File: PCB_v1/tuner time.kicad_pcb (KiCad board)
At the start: 4 copper layers, 60 x 40.5 mm, 130 parts, among them IC1 MIC_I2S_SPH0645, IC2 MIC_I2S_SPH0645, IC3 FT2332RL, J1 1051640001, J2 S2B-PH-K-SLFSN, J3 Conn_01x05_Pin, J4 Conn_01x05_Pin, J5 OLED Module Mount, SW7 SW_Push, SW8 SW_Push, U1 BQ25185DLHR, U2 BQ27441-G1, U3 DRV8834PWP, U4 STM32F407VGT6

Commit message: Initial placement draft
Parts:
- removed C32, C33, C34, C38, C39, C42: 100nF, Capacitor_SMD:C_0805_2012Metric
- removed C35, C36, C37: 1uF, Capacitor_SMD:C_0805_2012Metric
- removed C40, C41: 2.2uF, Capacitor_SMD:C_0805_2012Metric
- removed C43, C44: 20pF, Capacitor_SMD:C_0805_2012Metric
- removed C45, C46: 6.8pF, Capacitor_SMD:C_0805_2012Metric
- removed C47: .1uF, Capacitor_SMD:C_0805_2012Metric
- removed IC1, IC2: MIC_I2S_SPH0645, Parts_Library:SPH0645LM4H
- removed IC3: FT2332RL, Parts_Library:SSOP28-LD
- removed JP4, JP5: SB, Jumper:SolderJumper-2_P1.3mm_Bridged_Pad1.0x1.5mm
- removed L1: L, Inductor_SMD:L_0805_2012Metric
- removed R22, R23, R36, R40, R44: 10k, Resistor_SMD:R_0805_2012Metric
- removed R33: 1.5k, Resistor_SMD:R_0805_2012Metric
- removed R34, R35: 47k, Resistor_SMD:R_0805_2012Metric
- removed R37, R38: 0.10, Resistor_SMD:R_0805_2012Metric
- removed R39: 1, Resistor_SMD:R_0805_2012Metric
- removed R41, R45, R56: 510, Resistor_SMD:R_0805_2012Metric
- removed R42: 47, Resistor_SMD:R_0805_2012Metric
- removed R43, R48, R49, R50, R51, R52: 0, Resistor_SMD:R_0805_2012Metric
- removed R46: 330, Resistor_SMD:R_0805_2012Metric
- removed R47: 100, Resistor_SMD:R_0805_2012Metric
- removed R53: 220, Resistor_SMD:R_0805_2012Metric
- removed R54: 220k, Resistor_SMD:R_0805_2012Metric
- removed R55: 100k, Resistor_SMD:R_0805_2012Metric
- removed R57, R58, R59: 680, Resistor_SMD:R_0805_2012Metric
- removed REF**: CONN_B4B-XH-A_JST, Parts_Library:CONN_B4B-XH-A_JST
- added C22: 100nF, Capacitor_SMD:C_0805_2012Metric, F.Cu at (155.1, 75.8)
- added D7: Orange, LED_SMD:LED_0805_2012Metric_Pad1.15x1.40mm_HandSolder, F.Cu at (171.5, 104.6)
- added F1: MFU0805FF01000P500, Parts_Library:FUS_VISHAY_MFU0805_VIS, F.Cu at (154.0, 108.9)
- added FB1: FerriteBead, Inductor_SMD:L_0805_2012Metric, F.Cu at (175.6, 119.8)
- added J10: 1051640001, Parts_Library:CON00906_5_MOL, F.Cu at (155.8, 104.0)
- added J6: Conn_01x05_Pin, Connector_PinHeader_2.54mm:PinHeader_1x05_P2.54mm_Vertical, F.Cu at (225.6, 108.0)
- added J7: Conn_02x04_Odd_Even, Connector_PinHeader_2.00mm:PinHeader_2x04_P2.00mm_Vertical, F.Cu at (191.5, 137.5)
- added J8: B4B-XH-A, Parts_Library:JST_B4B-XH-A, F.Cu at (226.0, 119.0)
- added J9: Conn_ARM_JTAG_SWD_10, Connector_PinHeader_1.27mm:PinHeader_2x05_P1.27mm_Vertical, F.Cu at (186.0, 102.2)
- added JP1: M1, Jumper:SolderJumper-3_P1.3mm_Open_RoundedPad1.0x1.5mm, F.Cu at (191.2, 87.3)
- added JP2: M2, Jumper:SolderJumper-3_P1.3mm_Open_RoundedPad1.0x1.5mm, F.Cu at (191.2, 91.2)
- added RN1: 1k, Parts_Library:RESCAXE50P280X160X55-16N, F.Cu at (166.8, 130.9)
- added RN2: 10k, Parts_Library:RESCAXE50P280X160X55-16N, F.Cu at (171.2, 130.9)
- added RN3: 660, Parts_Library:RESCAXS80P320X160X60-8N, F.Cu at (203.2, 104.8)
- added RV1: 10k, Parts_Library:TRIM_TC33X-2-103E, F.Cu at (205.5, 118.0)
- added SW1: SW_SPST, Parts_Library:JST_B2B-XH-A, F.Cu at (154.0, 121.0)
- added SW2: SW_Push, GT_library:JST_B2B-PH-K-S, F.Cu at (178.5, 136.0)
- added SW3: SW_Push, GT_library:JST_B2B-PH-K-S, F.Cu at (173.5, 136.0)
- added SW4: SW_Push, GT_library:JST_B2B-PH-K-S, F.Cu at (168.5, 136.0)
- added SW5: SW_Push, GT_library:JST_B2B-PH-K-S, F.Cu at (163.5, 136.0)
- added SW6: SW_Push, GT_library:JST_B2B-PH-K-S, F.Cu at (158.5, 136.0)
- added SW9: SW_SPDT, Button_Switch_SMD:SW_SPDT_PCM12, F.Cu at (192.0, 103.5)
- added TP1: ~, TestPoint:TestPoint_THTPad_D1.0mm_Drill0.5mm, F.Cu at (202.5, 126.5)
- added TP10: ~, TestPoint:TestPoint_THTPad_D1.0mm_Drill0.5mm, F.Cu at (185.8, 113.0)
- added TP11: ~, TestPoint:TestPoint_THTPad_D1.0mm_Drill0.5mm, F.Cu at (126.7, 62.4)
- added TP12: ~, TestPoint:TestPoint_THTPad_D1.0mm_Drill0.5mm, F.Cu at (126.7, 65.5)
- added TP13: ~, TestPoint:TestPoint_THTPad_D1.0mm_Drill0.5mm, F.Cu at (183.8, 113.0)
- added TP2: ~, TestPoint:TestPoint_THTPad_D1.0mm_Drill0.5mm, F.Cu at (221.5, 116.5)
- added TP3: TestPoint, TestPoint:TestPoint_THTPad_D1.0mm_Drill0.5mm, F.Cu at (125.7, 101.0)
- added TP4: TestPoint, TestPoint:TestPoint_THTPad_D1.0mm_Drill0.5mm, F.Cu at (125.7, 104.1)
- added TP5: TestPoint, TestPoint:TestPoint_THTPad_D1.0mm_Drill0.5mm, F.Cu at (125.7, 107.1)
- added TP6: TestPoint, TestPoint:TestPoint_THTPad_D1.0mm_Drill0.5mm, F.Cu at (125.7, 110.2)
- added TP7: ~, TestPoint:TestPoint_THTPad_D1.0mm_Drill0.5mm, F.Cu at (120.6, 62.4)
- added TP8: ~, TestPoint:TestPoint_THTPad_D1.0mm_Drill0.5mm, F.Cu at (120.6, 65.5)
- added TP9: ~, TestPoint:TestPoint_THTPad_D1.0mm_Drill0.5mm, F.Cu at (123.6, 62.4)
- added U5: STM32F405RGTx, Package_QFP:LQFP-64_10x10mm_P0.5mm, F.Cu at (187.5, 122.8)
- added U6: ESD9B5.0ST5G, Parts_Library:SODFL1006X40N, F.Cu at (152.0, 108.0)
- added XTAL1: MC-306 32.7680K-E3:ROHS, Parts_Library:SO4_MC-306_SEC, F.Cu at (163.5, 87.7)
- added Y1: ASE-8MHz-L-C-T, Oscillator:Oscillator_SMD_Abracon_ASE-4Pin_3.2x2.5mm, F.Cu at (177.7, 112.9)
- C10: value 10uF -> 100uF; footprint Capacitor_SMD:C_0805_2012Metric -> Parts_Library:CAP_EEE1AA101WR
- C11, C2: value 1uF -> 10uF
- C12: value 0.47uF -> 0.1uF
- C13: value 1uF -> 0.1uF
- C14: value .1uF -> 10uF
- C15, C18: value .1uF -> 20pF
- C16: value .1uF -> 0.01uF
- C17: value .1uF -> 100nF
- C19: value .1uF -> 6.8pF
- C20: value 0.01uF -> 6.8pF
- C21: value 4.7uF -> 10uF
- C23, C26: value 10uF -> 100nF
- C24: value 0.1uF -> 100nF
- C25: value 0.1uF -> 2.2uF
- C27: value 100nF -> 2.2uF
- C3: value 220pF -> 1uF
- C30, C31: value 100nF -> 1uF
- C4: value 220pF -> 0.47uF
- C5: value 0.1uF -> 1uF
- C6: value 10uF -> 100nF; footprint Capacitor_SMD:C_0805_2012Metric -> GT_library:CAP_CA0612_3P2X1P6_YAG
- C7: value 0.1uF -> 100nF; footprint Capacitor_SMD:C_0805_2012Metric -> GT_library:CAP_CA0612_3P2X1P6_YAG
- C8: value 1uF -> 0.01uF
- C9: value 1uF -> 4.7uF
- D1, D2: value YELLOW -> Green
- D3: value Green -> Orange
- D4: value Orange -> Red
- D5: value Red -> Blue
- D6: value Blue -> Green
- J1: value 1051640001 -> Conn_01x03; footprint Parts_Library:CON00906_5_MOL -> Connector_PinHeader_2.54mm:PinHeader_1x03_P2.54mm_Vertical
- J2: value S2B-PH-K-SLFSN -> B6B-PH-K-S; footprint Parts_Library:CONN_S2B-PH-K-S_JST -> GT_library:JST_B6B-PH-K-S
- J3: value Conn_01x05_Pin -> B6B-PH-K-S; footprint Connector_PinHeader_1.00mm:PinHeader_1x05_P1.00mm_Vertical -> GT_library:JST_B6B-PH-K-S
- J4: value Conn_01x05_Pin -> S2B-PH-K-SLFSN; footprint Connector_PinHeader_1.00mm:PinHeader_1x05_P1.00mm_Vertical -> Parts_Library:CONN_S2B-PH-K-S_JST
- J5: value OLED Module Mount -> Conn_01x05_Pin; footprint Connector_PinHeader_2.54mm:PinHeader_1x11_P2.54mm_Vertical -> Connector_PinHeader_2.54mm:PinHeader_1x05_P2.54mm_Vertical
- JP3: value SB -> SLP; footprint Jumper:SolderJumper-2_P1.3mm_Bridged_Pad1.0x1.5mm -> Jumper:SolderJumper-3_P1.3mm_Bridged12_RoundedPad1.0x1.5mm
- R1: value 10k -> 680
- R10: value 0.01 1% -> 100
- R11: value 10k -> 100
- R12: value 1.1k -> 100
- R13, R8, R9: value 5.1k -> 100
- R14, R16, R17: value 100 -> 47k
- R15: value 100 -> 1.5k
- R18: value 100 -> 10k
- R19: value 100 -> 0.10
- R2: value 10k -> 5.1k
- R20: value 10k -> 0.10
- R21: value 10k -> 1
- R24: value 10k -> 220
- R25: value 10k -> 22
- R26, R27, R28: value 1k -> 22
- R29, R30: value 1k -> 10k
- R3: value 68 -> 5.1k
- R31: value 1k -> 680
- R32: value 47k -> 680
- R4: value 68 -> 0.01 1%
- R5: value 0 -> 10k
- R6: value 0 -> 1.1k
- R7: value 300 -> 5.1k
- SW7: footprint Button_Switch_SMD:SW_Push_1P1T_NO_CK_PTS125Sx43PSMTR -> GT_library:JST_B2B-PH-K-S
- SW8: footprint Button_Switch_SMD:SW_Push_1P1T_NO_CK_PTS125Sx43PSMTR -> Parts_Library:SW_TS04-66-65-BK-160-SMT
- U1: value BQ25185DLHR -> C1F 2; footprint Parts_Library:WSON10_DLH_TEX -> Parts_Library:C1_BEL
- U2: value BQ27441-G1 -> BQ25185DLHR; footprint Package_SON:Texas_S-PDSO-N12 -> Parts_Library:WSON10_DLH_TEX
- U3: value DRV8834PWP -> BQ27441-G1; footprint Parts_Library:SOP65P640X120-25N -> Package_SON:Texas_S-PDSO-N12
- U4: value STM32F407VGT6 -> DRV8834PWP; footprint Parts_Library:LQFP100_14x14_STM -> Parts_Library:SOP65P640X120-25N
- moved C17 121.7 mm to (93.5, 68.4)
- moved C19 121.7 mm to (93.5, 74.5)
- moved J2 108.6 mm to (206.5, 130.9), turned to 0 degrees
- moved U1 104.7 mm to (212.0, 108.5), turned to -90 degrees
- moved C25 99.1 mm to (97.9, 74.5)
- moved C8 98.3 mm to (136.8, 62.4)
- moved C20 94.4 mm to (93.5, 77.5)
- moved U4 93.3 mm to (216.2, 116.9), turned to 180 degrees
- moved R30 90.4 mm to (140.3, 143.0)
- moved C2 89.9 mm to (112.5, 115.8)
- moved C3 89.9 mm to (112.5, 118.8)
- moved C4 89.9 mm to (112.5, 121.8)
- moved R14 89.1 mm to (132.4, 62.4)
- moved J1 88.2 mm to (182.9, 137.0), turned to 90 degrees
- moved C27 88.0 mm to (102.4, 62.4)
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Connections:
- C1 pad 1: 3V3 -> GND
- C1 pad 2: GND -> Net-(SW1-A)
- C10 pad 1: VSYS -> VMOT
- C10 pad 2: GND -> AGND
- C11 pad 1: BATT_POS -> VMOT
- C11 pad 2: GND -> AGND
- C12 pad 1: Net-(U2-V_{DD}) -> VMOT
- C12 pad 2: GND -> AGND
- C13 pad 1: GND -> VMOT
- C13 pad 2: VBUS -> AGND
- C14 pad 1: Button1 -> Net-(C14-Pad1)
- C14 pad 2: GND -> AGND
- C15 pad 1: Button2 -> PH0-OSCIN
- C16 pad 1: Button3 -> +3.3V
- C17 pad 1: Button4 -> NRST
- C18 pad 1: Button5 -> PH1-OSCOUT
- C19 pad 1: Button6 -> PC14-OSC32IN
- C2 pad 1: 3V3 -> VSYS
- C20 pad 1: VMOT -> PC15-OSC32OUT
- C20 pad 2: Net-(U3-VCP) -> GND
- C21 pad 1: VINT -> +3.3V
- C23 pad 1: VMOT -> +3.3V
- C24 pad 1: VMOT -> +3.3V
- C25 pad 1: VMOT -> Net-(U5-VCAP_1)
- C26 pad 1: Net-(C26-Pad1) -> +3.3V
- C27 pad 1: GND -> Net-(U5-VCAP_2)
- C27 pad 2: 3V3 -> GND
- C28 pad 1: GND -> +3.3V
- C28 pad 2: 3V3 -> GND
- C29 pad 1: GND -> +3.3VA
- C29 pad 2: 3V3 -> GND
- C3 pad 1: 3V3 -> BATT_POS
- C30 pad 1: GND -> +3.3VA
- C30 pad 2: 3V3 -> GND
- C31 pad 1: GND -> +3.3V
- C31 pad 2: 3V3 -> GND
- C4 pad 1: 3V3 -> Net-(U3-V_{DD})
- C5 pad 1: VBUS -> GND
- C5 pad 2: GND -> VBUS
- C6 pad 1: VBUS -> GND
- C7 pad 1: 3V3 -> Net-(RN1H-R8.1)
- C7 pad 2: GND -> Net-(RN1G-R7.1)
- C8 pad 1: /USB to UART/DTR -> VMOT
- C8 pad 2: GND -> Net-(U4-VCP)
- C9 pad 1: GND -> 3V3
- C9 pad 2: BATT_POS -> AGND
- D1 pad 1: (no net) -> Net-(D1-K)
- D1 pad 2: (no net) -> /Motor/FLT
- D2 pad 1: (no net) -> Net-(D2-K)
- D2 pad 2: (no net) -> PC10
- D3 pad 1: GND -> Net-(D3-K)
- D3 pad 2: Net-(D3-A) -> PC11
- D4 pad 1: GND -> Net-(D4-K)
- D4 pad 2: Net-(D4-A) -> PC12
- D5 pad 1: GND -> Net-(D5-K)
- D5 pad 2: Net-(D5-A) -> PB4
- D6 pad 1: GND -> Net-(D6-K)
- D6 pad 2: Net-(D6-A) -> 3V3
- J1 pad 1: VBUS -> MCU_RX
- J1 pad 2: D- -> MCU_TX
- J1 pad 3: D+ -> GND
- J2 pad 1: GND -> 3V3
- J2 pad 2: BATT_POS -> I2S_WS
- J3 pad 1: unconnected-(J3-Pin_1-Pad1) -> GND
- J3 pad 2: unconnected-(J3-Pin_2-Pad2) -> I2S_WS
- J3 pad 3: Net-(J3-Pin_3) -> I2S_DATA
- J3 pad 4: Net-(J3-Pin_4) -> I2S_BCLK
- J3 pad 5: Net-(J3-Pin_5) -> GND
- J4 pad 1: unconnected-(J4-Pin_1-Pad1) -> GND
- J4 pad 2: unconnected-(J4-Pin_2-Pad2) -> Net-(SW1-A)
- J5 pad 1: MOSI -> unconnected-(J5-Pin_1-Pad1)
- J5 pad 2: SCK -> unconnected-(J5-Pin_2-Pad2)
- J5 pad 3: DC -> Net-(J5-Pin_3)
- J5 pad 4: RST -> Net-(J5-Pin_4)
- J5 pad 5: CS -> Net-(J5-Pin_5)
- JP3 pad 1: Net-(JP3-A) -> 5V
- JP3 pad 2: GND -> /Motor/SLP
- R1 pad 1: GND -> Net-(D1-K)
- R1 pad 2: Net-(IC1-SELECT) -> GND
- R10 pad 1: BATT_POS -> VSYS
- R10 pad 2: VSYS -> Net-(J6-Pin_3)
- R11 pad 1: Net-(U2-BIN) -> 3V3
- R11 pad 2: GND -> Net-(J5-Pin_5)
- R12 pad 1: Net-(U1-ILIM/VSET) -> GND
- R12 pad 2: GND -> Net-(J5-Pin_4)
- R13 pad 1: 3V3 -> VSYS
- R13 pad 2: Net-(U2-GPOUT) -> Net-(J5-Pin_3)
- R14 pad 1: 5V -> 3V3
- R14 pad 2: Net-(J4-Pin_5) -> Net-(U4-CONFIG)
- R15 pad 1: GND -> Net-(U4-FAULT)
- R15 pad 2: Net-(J4-Pin_4) -> /Motor/FLT
- R16 pad 1: VSYS -> Net-(U4-BDECAY)
- R16 pad 2: Net-(J4-Pin_3) -> AGND
- R17 pad 1: 3V3 -> Net-(U4-ADECAY)
- R17 pad 2: Net-(J3-Pin_5) -> AGND
- R18 pad 1: GND -> /Motor/FLT
- R18 pad 2: Net-(J3-Pin_4) -> /Motor/SLP
- R19 pad 1: VSYS -> Net-(U4-BAISEN)
- R19 pad 2: Net-(J3-Pin_3) -> AGND
- R2 pad 2: Net-(IC2-SELECT) -> SCL
- R20 pad 1: 3V3 -> Net-(U4-AISEN)
- R20 pad 2: Net-(R20-Pad2) -> AGND
- R21 pad 1: 3V3 -> VMOT
- R21 pad 2: Net-(R21-Pad2) -> Net-(C14-Pad1)
- R24 pad 1: 3V3 -> Net-(Y1-OUT)
- R24 pad 2: Net-(R24-Pad2) -> PH1-OSCOUT
- R25 pad 1: 3V3 -> NRST
- R25 pad 2: Net-(R25-Pad2) -> Net-(J9-~{RESET})
- R26 pad 1: Net-(R20-Pad2) -> SWCLK
- R26 pad 2: Button1 -> Net-(J9-SWCLK/TCK)
- R27 pad 1: Net-(R21-Pad2) -> SWDIO
- R27 pad 2: Button2 -> Net-(J9-SWDIO/TMS)
- R28 pad 1: Net-(R22-Pad2) -> SWO
- R28 pad 2: Button3 -> Net-(J9-SWO/TDO)
- R29 pad 2: Button4 -> BOOT0
- R3 pad 1: Net-(IC1-DATA) -> 3V3
- R3 pad 2: /Mic/DATA -> SDA
- R30 pad 1: Net-(R24-Pad2) -> /MCU/BOOT1
- R30 pad 2: Button5 -> GND
- R31 pad 1: Net-(R25-Pad2) -> GND
- R31 pad 2: Button6 -> Net-(D7-K)
- R32 pad 1: VINT -> GND
- R32 pad 2: Net-(JP1-B) -> Net-(D6-K)
- R4 pad 1: Net-(IC2-DATA) -> BATT_POS
- R4 pad 2: /Mic/DATA -> VSYS
- R5 pad 1: Net-(IC3-USBDP) -> Net-(U3-BIN)
- R5 pad 2: D+ -> GND
- R6 pad 1: Net-(IC3-USBDM) -> Net-(U2-ILIM/VSET)
- R6 pad 2: D- -> GND
- R7 pad 1: Net-(D1-PadA) -> 3V3
- R7 pad 2: VBUS -> Net-(U3-GPOUT)
- R8 pad 1: 3V3 -> 5V
- R8 pad 2: SCL -> Net-(J6-Pin_5)
- R9 pad 1: 3V3 -> AGND
- R9 pad 2: SDA -> Net-(J6-Pin_4)
- SW7 pad 1: 3V3 -> GND
- U1 pad 1: VSYS -> 5V
- U1 pad 2: BATT_POS -> VMOT
- U2 pad 1: SDA -> VSYS
- U2 pad 10: Net-(U2-BIN) -> VBUS
- U2 pad 11: unconnected-(U2-NC-Pad11) -> GND
- U2 pad 2: SCL -> BATT_POS
- U2 pad 3: GND -> unconnected-(U2-STAT2-Pad3)
- U2 pad 4: unconnected-(U2-NC-Pad4) -> GND
- U2 pad 5: Net-(U2-V_{DD}) -> GND
- U2 pad 6: BATT_POS -> GND
- U2 pad 7: VSYS -> Net-(U2-ILIM/VSET)
- U2 pad 8: BATT_POS -> Net-(U2-ILIM/VSET)
- U3 pad 1: Net-(U3-AOUT1) -> SDA
- U3 pad 10: /Motor/M0 -> Net-(U3-BIN)
- U3 pad 11: /Motor/M1 -> unconnected-(U3-NC-Pad11)
- U3 pad 12: Net-(JP1-B) -> Net-(U3-GPOUT)
- U3 pad 13: Net-(U3-FAULT) -> GND
- U3 pad 2: Net-(U3-AISEN) -> SCL
- U3 pad 3: Net-(U3-AOUT2) -> GND
- U3 pad 4: Net-(M1--) -> unconnected-(U3-NC-Pad4)
- U3 pad 5: Net-(U3-BAISEN) -> Net-(U3-V_{DD})
- U3 pad 6: Net-(U3-BOUT1) -> BATT_POS
- U3 pad 7: /Motor/EN -> VSYS
- U3 pad 8: /Motor/STEP -> BATT_POS
- U3 pad 9: /Motor/DIR -> unconnected-(U3-NC-Pad9)
- U4 pad 1: unconnected-(U4B-PE2-Pad1) -> /Motor/A1
- U4 pad 10: GND -> /Motor/M0
- U4 pad 11: 3V3 -> /Motor/M1
- U4 pad 12: PH0-OSCIN -> Net-(U4-CONFIG)
- U4 pad 13: PH1-OSCOUT -> Net-(U4-FAULT)
- U4 pad 14: NRST -> Net-(U4-VCP)
- U4 pad 15: unconnected-(U4A-PC0-Pad15) -> VMOT
- U4 pad 16: unconnected-(U4A-PC1-Pad16) -> VMOT
- U4 pad 17: unconnected-(U4A-PC2-Pad17) -> 3V3
- U4 pad 18: unconnected-(U4A-PC3-Pad18) -> AGND
- U4 pad 19: 3V3 -> /Motor/VREF
- U4 pad 2: unconnected-(U4B-PE3-Pad2) -> Net-(U4-AISEN)
- U4 pad 20: unconnected-(U4C-VSSA-Pad20) -> /Motor/VREF
- U4 pad 21: VREF+ -> Net-(U4-VREF0)
- U4 pad 22: Net-(U4C-VDDA) -> /Motor/SLP
- U4 pad 23: PA0 -> Net-(U4-BDECAY)
- U4 pad 24: unconnected-(U4A-PA1-Pad24) -> Net-(U4-ADECAY)
- U4 pad 25: unconnected-(U4A-PA2-Pad25) -> AGND
- U4 pad 3: unconnected-(U4B-PE4-Pad3) -> /Motor/A2
- U4 pad 4: unconnected-(U4B-PE5-Pad4) -> /Motor/B2
- U4 pad 5: unconnected-(U4B-PE6-Pad5) -> Net-(U4-BAISEN)
- U4 pad 6: Net-(U4C-VBAT) -> /Motor/B1
- U4 pad 7: unconnected-(U4A-PC13-Pad7) -> /Motor/EN
- U4 pad 8: PC14-OSC32IN -> STEP
- U4 pad 9: PC15-OSC32OUT -> DIR
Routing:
- net STEP: track 0.00 -> 2.93 mm
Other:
- board size 60 x 40.5 mm -> 80 x 40 mm

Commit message: bringing back the PCB to Life
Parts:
- moved C27 113.8 mm to (202.5, 116.5)
- moved C25 111.7 mm to (196.0, 128.0), turned to -90 degrees
- moved R14 104.6 mm to (221.0, 118.0), turned to 180 degrees
- moved C8 91.3 mm to (212.9, 113.0), turned to 90 degrees
- moved C17 87.1 mm to (153.5, 131.5)
- moved R21 82.3 mm to (208.0, 115.5), turned to 90 degrees
- moved TP10 69.9 mm to (117.2, 126.9)
- moved C19 68.3 mm to (125.2, 134.9), turned to -90 degrees
- moved TP9 64.6 mm to (186.3, 78.0)
- moved TP7 64.6 mm to (183.3, 78.0)
- moved TP8 64.6 mm to (183.3, 81.1)
- moved TP11 64.6 mm to (189.4, 78.0)
- moved TP12 64.6 mm to (189.4, 81.1)
- moved C23 64.5 mm to (199.5, 125.5)
- moved XTAL1 62.9 mm to (119.7, 132.9)
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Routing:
- net STEP: track 2.93 -> 0.00 mm
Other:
- board text added: "goes on the back"

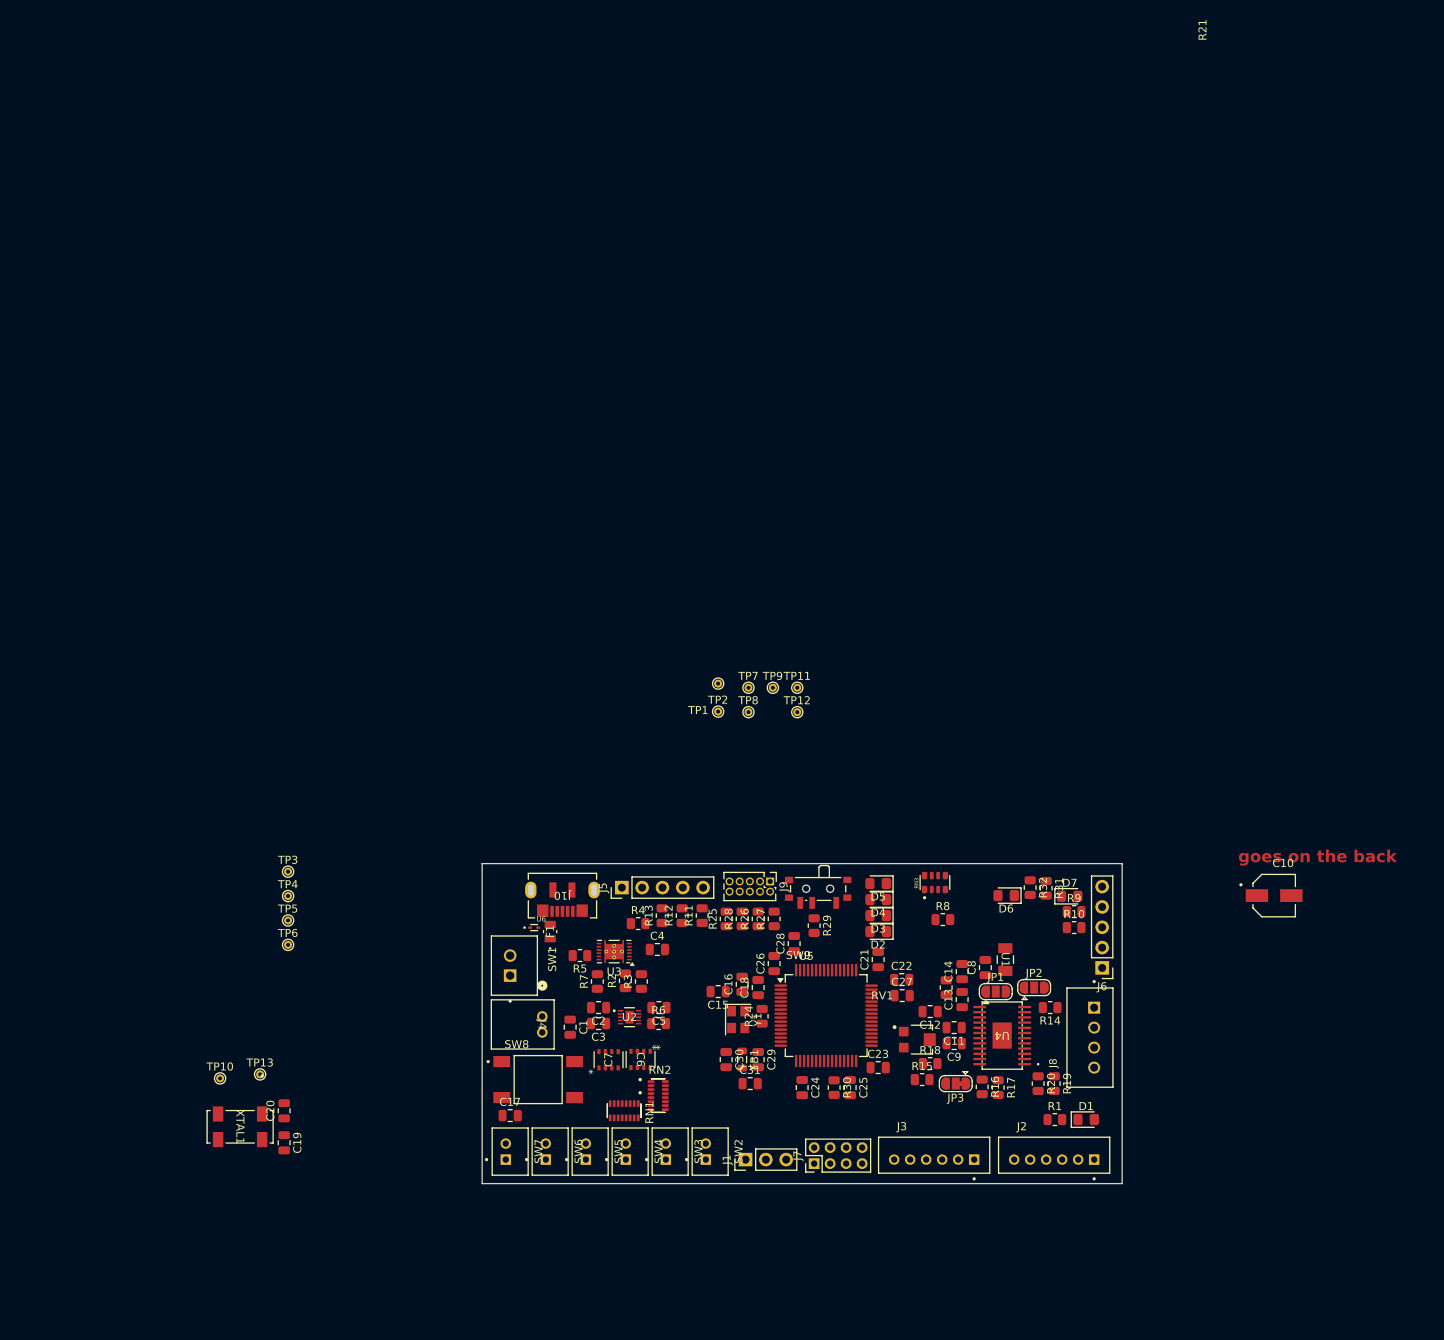
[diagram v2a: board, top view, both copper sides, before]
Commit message: adjusted placments
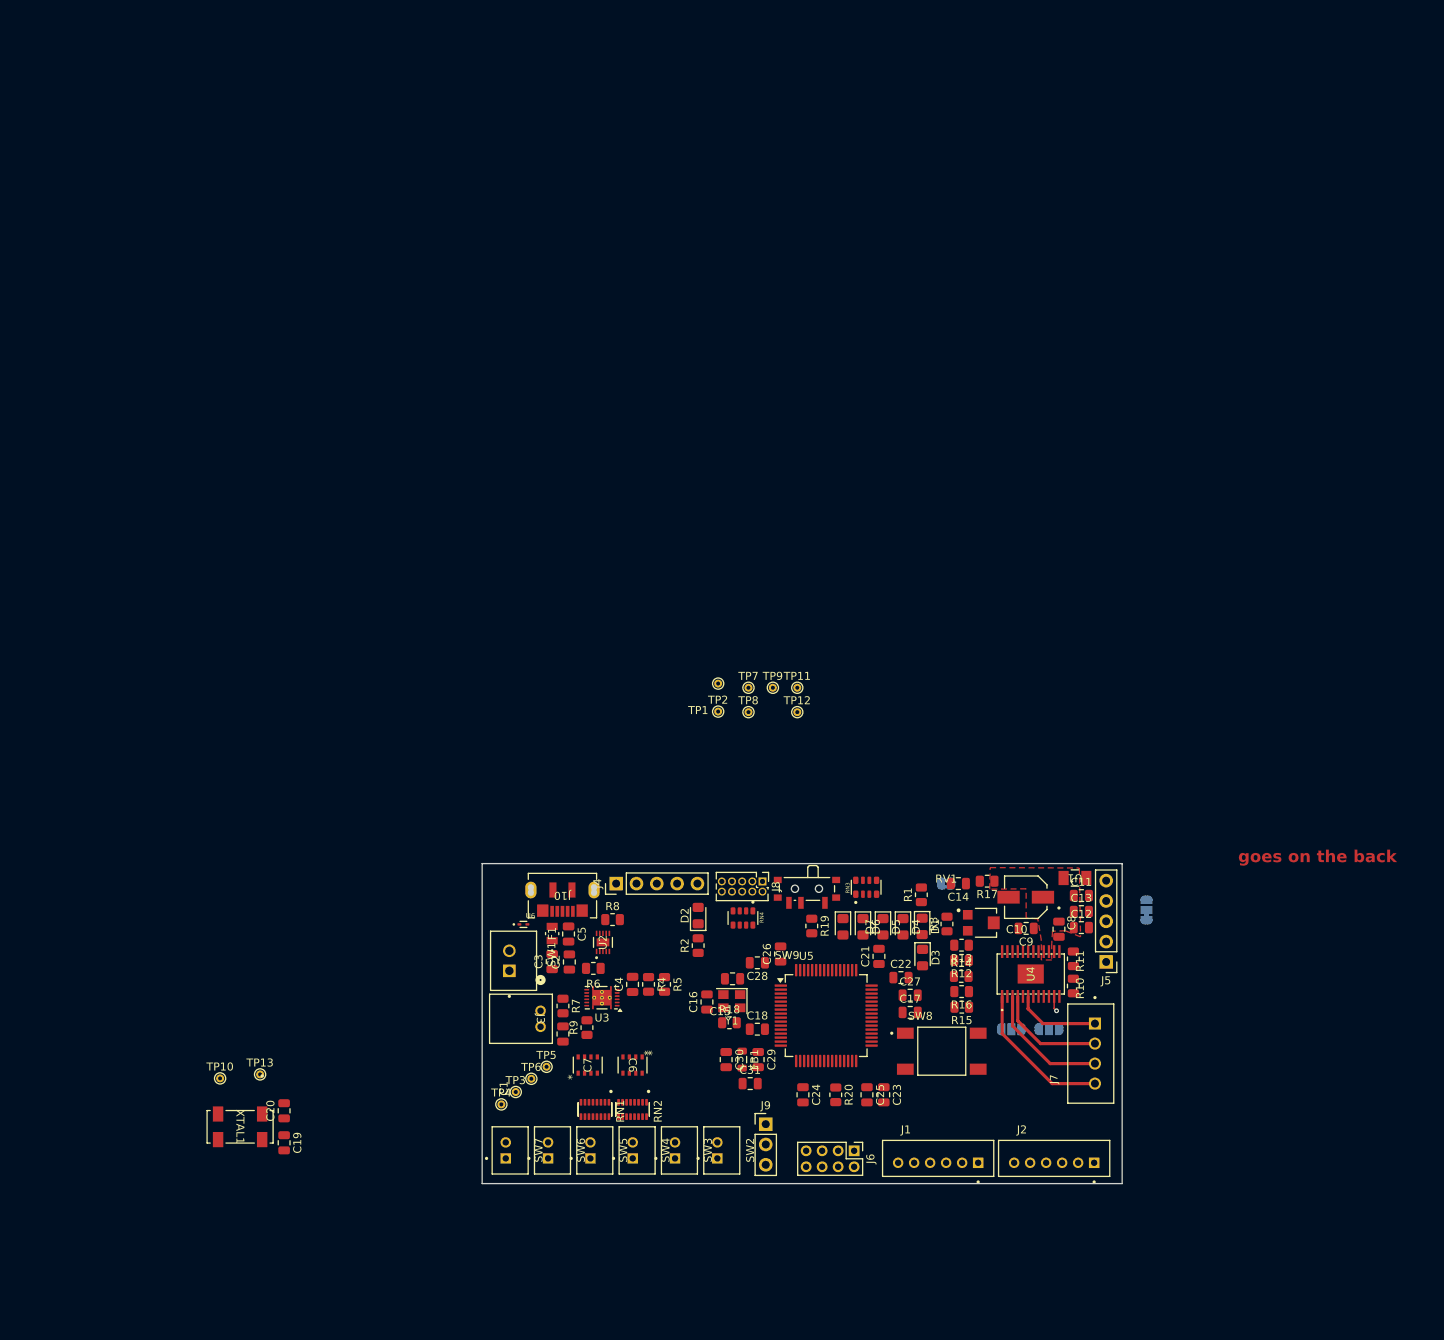
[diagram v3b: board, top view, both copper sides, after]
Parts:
- removed R21: 1, Resistor_SMD:R_0805_2012Metric
- removed R24: 220, Resistor_SMD:R_0805_2012Metric
- removed R25, R26, R27, R28: 22, Resistor_SMD:R_0805_2012Metric
- removed R29, R30: 10k, Resistor_SMD:R_0805_2012Metric
- removed R31, R32: 680, Resistor_SMD:R_0805_2012Metric
- added JP4: SLP, Jumper:SolderJumper-3_P1.3mm_Bridged12_RoundedPad1.0x1.5mm, B.Cu at (233.0, 105.8)
- added RN4: 22, Parts_Library:RESCAXE80P320X160X70-8N, F.Cu at (182.6, 106.8)
- D1: value Green -> Orange
- D3: value Orange -> Green
- D4: value Red -> Green
- D5: value Blue -> Orange
- D6: value Green -> Red
- D7: value Orange -> Blue
- J1: value Conn_01x03 -> B6B-PH-K-S; footprint Connector_PinHeader_2.54mm:PinHeader_1x03_P2.54mm_Vertical -> GT_library:JST_B6B-PH-K-S
- J3: value B6B-PH-K-S -> S2B-PH-K-SLFSN; footprint GT_library:JST_B6B-PH-K-S -> Parts_Library:CONN_S2B-PH-K-S_JST
- J4: value S2B-PH-K-SLFSN -> Conn_01x05_Pin; footprint Parts_Library:CONN_S2B-PH-K-S_JST -> Connector_PinHeader_2.54mm:PinHeader_1x05_P2.54mm_Vertical
- J6: value Conn_01x05_Pin -> Conn_02x04_Odd_Even; footprint Connector_PinHeader_2.54mm:PinHeader_1x05_P2.54mm_Vertical -> Connector_PinHeader_2.00mm:PinHeader_2x04_P2.00mm_Vertical
- J7: value Conn_02x04_Odd_Even -> B4B-XH-A; footprint Connector_PinHeader_2.00mm:PinHeader_2x04_P2.00mm_Vertical -> Parts_Library:JST_B4B-XH-A
- J8: value B4B-XH-A -> Conn_ARM_JTAG_SWD_10; footprint Parts_Library:JST_B4B-XH-A -> Connector_PinHeader_1.27mm:PinHeader_2x05_P1.27mm_Vertical
- J9: value Conn_ARM_JTAG_SWD_10 -> Conn_01x03; footprint Connector_PinHeader_1.27mm:PinHeader_2x05_P1.27mm_Vertical -> Connector_PinHeader_2.54mm:PinHeader_1x03_P2.54mm_Vertical
- JP1: value M1 -> SolderJumper_2_Bridged; footprint Jumper:SolderJumper-3_P1.3mm_Open_RoundedPad1.0x1.5mm -> Jumper:SolderJumper-2_P1.3mm_Bridged2Bar_RoundedPad1.0x1.5mm; moved to B.Cu
- JP2: value M2 -> M1; moved to B.Cu
- JP3: value SLP -> M2; footprint Jumper:SolderJumper-3_P1.3mm_Bridged12_RoundedPad1.0x1.5mm -> Jumper:SolderJumper-3_P1.3mm_Open_RoundedPad1.0x1.5mm; moved to B.Cu
- R10, R12, R13: value 100 -> 47k
- R11: value 100 -> 1.5k
- R14: value 47k -> 10k
- R15: value 1.5k -> 0.10
- R16: value 47k -> 0.10
- R17: value 47k -> 1
- R18: value 10k -> 220
- R19, R20: value 0.10 -> 10k
- R2, R3: value 5.1k -> 680
- R4: value 0.01 1% -> 5.1k
- R5: value 10k -> 5.1k
- R6: value 1.1k -> 0.01 1%
- R7: value 5.1k -> 10k
- R8: value 100 -> 1.1k
- R9: value 100 -> 5.1k
- moved R9 62.6 mm to (163.1, 120.5), turned to 90 degrees
- moved J5 61.2 mm to (228.0, 112.3), turned to 180 degrees
- moved J3 52.4 mm to (157.3, 118.4), turned to -90 degrees
- moved C17 51.6 mm to (203.5, 118.6)
- moved SW8 50.6 mm to (207.4, 123.5)
- moved R11 46.7 mm to (223.9, 111.9), turned to -90 degrees
- moved J8 45.4 mm to (185.0, 102.2), turned to -90 degrees
- moved R8 41.3 mm to (166.3, 107.0)
- moved TP3 39.6 mm to (154.2, 128.6)
- moved R3 38.9 mm to (208.1, 107.5)
- moved J6 38.5 mm to (196.5, 135.9), turned to -90 degrees
- moved R13 37.6 mm to (209.9, 110.2), turned to 180 degrees
- moved TP4 37.3 mm to (152.4, 130.1)
- moved J7 37.2 mm to (226.1, 123.8)
- moved TP5 37.1 mm to (158.1, 125.4)
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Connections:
- C6 pad 5: Button4 -> Button1
- C6 pad 6: Button3 -> Button2
- C6 pad 7: Button2 -> Button3
- C6 pad 8: Button1 -> Button4
- D1 pad 2: /Motor/FLT -> 5V
- D2 pad 2: PC10 -> 3V3
- D3 pad 2: PC11 -> /Motor/FLT
- D4 pad 2: PC12 -> PC10
- D5 pad 2: PB4 -> PC11
- D6 pad 2: 3V3 -> PC12
- D7 pad 2: 5V -> PB4
- J1 pad 1: MCU_RX -> 3V3
- J1 pad 2: MCU_TX -> I2S_WS
- J1 pad 3: GND -> I2S_DATA
- J2 pad 1: 3V3 -> GND
- J3 pad 2: I2S_WS -> Net-(SW1-A)
- J4 pad 1: GND -> unconnected-(J4-Pin_1-Pad1)
- J4 pad 2: Net-(SW1-A) -> unconnected-(J4-Pin_2-Pad2)
- J5 pad 3: Net-(J5-Pin_3) -> VSYS
- J5 pad 4: Net-(J5-Pin_4) -> AGND
- J5 pad 5: Net-(J5-Pin_5) -> 5V
- J6 pad 1: unconnected-(J6-Pin_1-Pad1) -> GND
- J6 pad 2: unconnected-(J6-Pin_2-Pad2) -> 3V3
- J6 pad 3: Net-(J6-Pin_3) -> MISO
- J6 pad 4: Net-(J6-Pin_4) -> CS
- J6 pad 5: Net-(J6-Pin_5) -> RST
- J7 pad 1: GND -> /Motor/B1
- J7 pad 2: 5V -> /Motor/B2
- J7 pad 3: MISO -> /Motor/A2
- J7 pad 4: CS -> /Motor/A1
- J8 pad 1: /Motor/B1 -> +3.3V
- J8 pad 2: /Motor/B2 -> Net-(J8-SWDIO/TMS)
- J8 pad 3: /Motor/A2 -> GND
- J8 pad 4: /Motor/A1 -> Net-(J8-SWCLK/TCK)
- J9 pad 1: +3.3V -> MCU_RX
- J9 pad 2: Net-(J9-SWDIO/TMS) -> MCU_TX
- JP1 pad 1: 5V -> AGND
- JP1 pad 2: /Motor/M1 -> GND
- JP2 pad 1: 5V -> 3V3
- JP2 pad 2: /Motor/M0 -> /Motor/M1
- JP3 pad 1: 5V -> 3V3
- JP3 pad 2: /Motor/SLP -> /Motor/M0
- R1 pad 1: Net-(D1-K) -> GND
- R1 pad 2: GND -> Net-(D1-K)
- R10 pad 1: VSYS -> 3V3
- R10 pad 2: Net-(J6-Pin_3) -> Net-(U4-CONFIG)
- R11 pad 1: 3V3 -> Net-(U4-FAULT)
- R11 pad 2: Net-(J5-Pin_5) -> /Motor/FLT
- R12 pad 1: GND -> Net-(U4-BDECAY)
- R12 pad 2: Net-(J5-Pin_4) -> AGND
- R13 pad 1: VSYS -> Net-(U4-ADECAY)
- R13 pad 2: Net-(J5-Pin_3) -> AGND
- R14 pad 1: 3V3 -> /Motor/FLT
- R14 pad 2: Net-(U4-CONFIG) -> /Motor/SLP
- R15 pad 1: Net-(U4-FAULT) -> Net-(U4-BAISEN)
- R15 pad 2: /Motor/FLT -> AGND
- R16 pad 1: Net-(U4-BDECAY) -> Net-(U4-AISEN)
- R17 pad 1: Net-(U4-ADECAY) -> VMOT
- R17 pad 2: AGND -> Net-(C14-Pad1)
- R18 pad 1: /Motor/FLT -> Net-(Y1-OUT)
- R18 pad 2: /Motor/SLP -> PH1-OSCOUT
- R19 pad 1: Net-(U4-BAISEN) -> Net-(SW9-B)
- R19 pad 2: AGND -> BOOT0
- R2 pad 1: 3V3 -> GND
- R2 pad 2: SCL -> Net-(D2-K)
- R20 pad 1: Net-(U4-AISEN) -> /MCU/BOOT1
- R20 pad 2: AGND -> GND
- R3 pad 1: 3V3 -> Net-(D3-K)
- R3 pad 2: SDA -> AGND
- R4 pad 1: BATT_POS -> 3V3
- R4 pad 2: VSYS -> SCL
- R5 pad 1: Net-(U3-BIN) -> 3V3
- R5 pad 2: GND -> SDA
- R6 pad 1: Net-(U2-ILIM/VSET) -> BATT_POS
- R6 pad 2: GND -> VSYS
- R7 pad 1: 3V3 -> Net-(U3-BIN)
- R7 pad 2: Net-(U3-GPOUT) -> GND
- R8 pad 1: 5V -> Net-(U2-ILIM/VSET)
- R8 pad 2: Net-(J6-Pin_5) -> GND
- R9 pad 1: AGND -> 3V3
- R9 pad 2: Net-(J6-Pin_4) -> Net-(U3-GPOUT)
- RN3 pad 1: Net-(D2-K) -> Net-(D7-K)
- RN3 pad 2: Net-(D3-K) -> Net-(D6-K)
- RN3 pad 3: Net-(D4-K) -> Net-(D5-K)
- RN3 pad 4: Net-(D5-K) -> Net-(D4-K)
- RV1 pad 1: Net-(U4-VREF0) -> AGND
- RV1 pad 3: AGND -> Net-(U4-VREF0)
- TP10 pad 1: PC14-OSC32IN -> Net-(U5-PC8)
- TP11 pad 1: Net-(U5-PB8) -> Net-(U5-PC7)
- TP12 pad 1: Net-(U5-PB9) -> Net-(U5-PB8)
- TP13 pad 1: PC15-OSC32OUT -> Net-(U5-PB9)
- TP7 pad 1: Net-(U5-PC9) -> PC14-OSC32IN
- TP8 pad 1: Net-(U5-PC8) -> PC15-OSC32OUT
- TP9 pad 1: Net-(U5-PC7) -> Net-(U5-PC9)
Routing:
- net /Motor/A1: track 0.00 -> 18.8 mm
- net /Motor/A2: track 0.00 -> 15.9 mm
- net /Motor/B2: track 0.00 -> 13.9 mm
- net /Motor/B1: track 0.00 -> 10.7 mm
- net /Motor/M1: track 0.00 -> 1.92 mm, vias 0 -> 1
- added copper zone on F.Cu, net VMOT
